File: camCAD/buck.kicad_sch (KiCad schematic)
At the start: 19 parts, among them J1 USB C Charging Port, J3 BATTERY, U1 BQ24072RGTR Charging IC, U2 SC189ZSKTRT

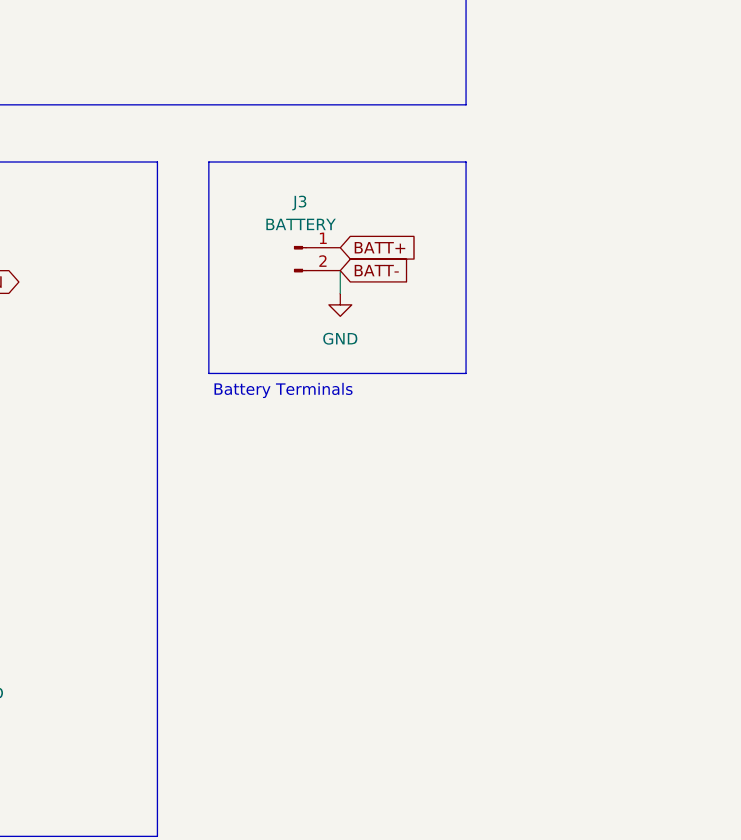
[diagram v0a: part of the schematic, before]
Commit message: Added user interface schematic and updated "camCAD/README.md"
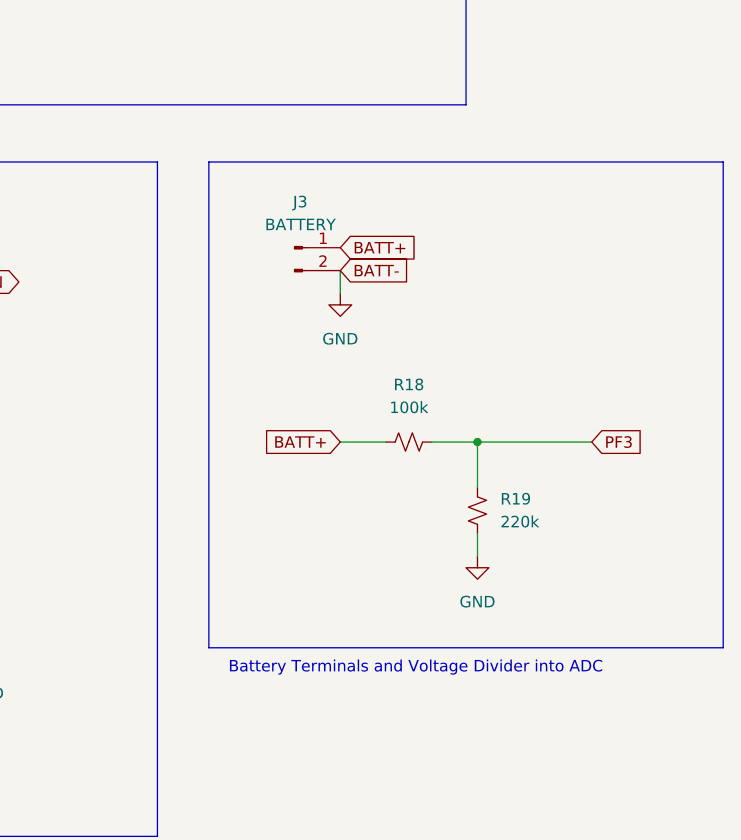
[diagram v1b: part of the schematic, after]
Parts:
- added R18: 100k, Resistor_SMD:R_0402_1005Metric, symbol Device:R_Small_US
- added R19: 220k, Resistor_SMD:R_0805_2012Metric, symbol Device:R_Small_US
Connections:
- net BATT+: now also R18.1
- net BQ_CHG: now also D7.C (K); no longer D7.1 (K)
- net BQ_PGOOD: now also D6.C (K); no longer D6.1 (K)
- net GND: now also R19.2
- net at R10.2: now also D6.A; no longer D6.2 (A)
- net at R12.2: now also D7.A; no longer D7.2 (A)
- new net PF3: R18.2, R19.1
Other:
- note added: "Battery Terminals and Voltage Divider into ADC"
- note removed: "Battery Terminals"

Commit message: Random push ishan karne
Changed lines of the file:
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@@
-	(wire
-		(pts
-			(xy 100.33 36.83) (xy 116.84 36.83)
-		)
-		(stroke
-			(width 0)
-			(type default)
-		)
-	)
 	(wire
 		(pts
@@
 		(property "Intersheetrefs" "${INTERSHEET_REFS}"
 			(at 110.5724 49.53 0)
+			(hide yes)
+			(show_name no)
+			(do_not_autoplace no)
+			(effects
+				(font
+					(size 1.27 1.27)
+				)
+				(justify left)
+			)
+		)
+	)
+	(global_label "BQ_VSS"
+		(shape input)
+		(at 100.33 36.83 0)
+		(fields_autoplaced yes)
+		(effects
+			(font
+				(size 1.27 1.27)
+			)
+			(justify left)
+		)
+		(property "Intersheetrefs" "${INTERSHEET_REFS}"
+			(at 110.3909 36.83 0)
 			(hide yes)
 			(show_name no)
@@
 					(unit 1)
 				)
-			)
-		)
-	)
-	(symbol
-		(lib_id "power:GND")
-		(at 116.84 36.83 0)
-		(unit 1)
-		(body_style 1)
-		(exclude_from_sim no)
-		(in_bom yes)
-		(on_board yes)
-		(in_pos_files yes)
-		(dnp no)
-		(fields_autoplaced yes)
-		(property "Reference" "#PWR06"
-			(at 116.84 43.18 0)
-			(hide yes)
-			(show_name no)
-			(do_not_autoplace no)
-			(effects
-				(font
-					(size 1.27 1.27)
-				)
-			)
-		)
-		(property "Value" "GND"
-			(at 116.84 41.91 0)
-			(show_name no)
-			(do_not_autoplace no)
-			(effects
-				(font
-					(size 1.27 1.27)
-				)
-			)
-		)
-		(property "Footprint" ""
-			(at 116.84 36.83 0)
-			(hide yes)
-			(show_name no)
-			(do_not_autoplace no)
-			(effects
-				(font
-					(size 1.27 1.27)
-				)
-			)
-		)
-		(property "Datasheet" ""
-			(at 116.84 36.83 0)
-			(hide yes)
-			(show_name no)
-			(do_not_autoplace no)
-			(effects
-				(font
-					(size 1.27 1.27)
-				)
-			)
-		)
-		(property "Description" "Power symbol creates a global label with name \"GND\" , ground"
-			(at 116.84 36.83 0)
-			(hide yes)
-			(show_name no)
-			(do_not_autoplace no)
-			(effects
-				(font
-					(size 1.27 1.27)
-				)
-			)
-		)
-		(pin "1"
-		)
-		(instances
-			(project "camCAD"
-				(path "/e2824ea6-9024-4cee-b80c-5fefbc7112d7/d4928a95-01f6-4ac1-a577-561f178a5e0e"
-					(reference "#PWR06")
-					(unit 1)
-				)

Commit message: layout partially complete
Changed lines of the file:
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@@
+	)
+	(junction
+		(at 219.71 82.55)
+		(diameter 0)
+		(color 0 0 0 0)
 	)
 	(junction
@@
 	(wire
 		(pts
+			(xy 224.79 80.01) (xy 224.79 76.2)
+		)
+		(stroke
+			(width 0)
+			(type default)
+		)
+	)
+	(wire
+		(pts
+			(xy 214.63 80.01) (xy 224.79 80.01)
+		)
+		(stroke
+			(width 0)
+			(type default)
+		)
+	)
+	(wire
+		(pts
 			(xy 163.83 83.82) (xy 156.21 83.82)
 		)
@@
 	(wire
 		(pts
+			(xy 219.71 82.55) (xy 214.63 82.55)
+		)
+		(stroke
+			(width 0)
+			(type default)
+		)
+	)
+	(wire
+		(pts
 			(xy 140.97 30.48) (xy 144.78 30.48)
 		)
@@
 	(wire
 		(pts
+			(xy 219.71 82.55) (xy 219.71 85.09)
+		)
+		(stroke
+			(width 0)
+			(type default)
+		)
+	)
+	(wire
+		(pts
 			(xy 113.03 101.6) (xy 113.03 105.41)
 		)
@@
 	(wire
 		(pts
+			(xy 224.79 76.2) (xy 227.33 76.2)
+		)
+		(stroke
+			(width 0)
+			(type default)
+		)
+	)
+	(wire
+		(pts
 			(xy 153.67 38.1) (xy 153.67 33.02)
 		)
@@
 	(wire
 		(pts
-			(xy 214.63 82.55) (xy 214.63 85.09)
-		)
-		(stroke
-			(width 0)
-			(type default)
-		)
-	)
-	(wire
-		(pts
 			(xy 175.26 106.68) (xy 175.26 114.3)
 		)
@@
 		(pts
 			(xy 175.26 121.92) (xy 175.26 124.46)
+		)
+		(stroke
+			(width 0)
+			(type default)
+		)
+	)
+	(wire
+		(pts
+			(xy 219.71 82.55) (xy 226.06 82.55)
 		)
 		(stroke
@@
 	(global_label "BATT+"
 		(shape input)
-		(at 214.63 80.01 0)
+		(at 227.33 76.2 0)
 		(fields_autoplaced yes)
 		(effects
@@
 		)
 		(property "Intersheetrefs" "${INTERSHEET_REFS}"
-			(at 223.4814 80.01 0)
+			(at 236.1814 76.2 0)
 			(hide yes)
 			(show_name no)
@@
 	(global_label "BATT-"
 		(shape input)
-		(at 214.63 82.55 0)
+		(at 226.06 82.55 0)
 		(fields_autoplaced yes)
 		(effects
@@
 		)
 		(property "Intersheetrefs" "${INTERSHEET_REFS}"
-			(at 223.4814 82.55 0)
+			(at 234.9114 82.55 0)
 			(hide yes)
 			(show_name no)
@@
 	(symbol
 		(lib_id "power:GND")
-		(at 214.63 85.09 0)
+		(at 219.71 85.09 0)
 		(unit 1)
 		(body_style 1)
@@
 		(fields_autoplaced yes)
 		(property "Reference" "#PWR017"
-			(at 214.63 91.44 0)
+			(at 219.71 91.44 0)
 			(hide yes)
 			(show_name no)
@@
 		)
 		(property "Value" "GND"
-			(at 214.63 90.17 0)
+			(at 219.71 90.17 0)
 			(show_name no)
 			(do_not_autoplace no)
@@
 		)
 		(property "Footprint" ""
-			(at 214.63 85.09 0)
+			(at 219.71 85.09 0)
 			(hide yes)
 			(show_name no)
@@
 		)
 		(property "Datasheet" ""
-			(at 214.63 85.09 0)
+			(at 219.71 85.09 0)
 			(hide yes)
 			(show_name no)
@@
 		)
 		(property "Description" "Power symbol creates a global label with name \"GND\" , ground"
-			(at 214.63 85.09 0)
-			(hide yes)
-			(show_name no)
+			(at 219.71 85.09 0)
+			(hide yes)
+			(show_name no)
